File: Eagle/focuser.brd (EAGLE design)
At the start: 52 x 110.2 mm, 50 parts, among them IC1 78xx, J1 J5MM, J10 J5MM, J2 J7MM, J3 J7MM, J4 J5MM, J5 J7MM, J6 J12MM, J7 J7MM, J8 J7MM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

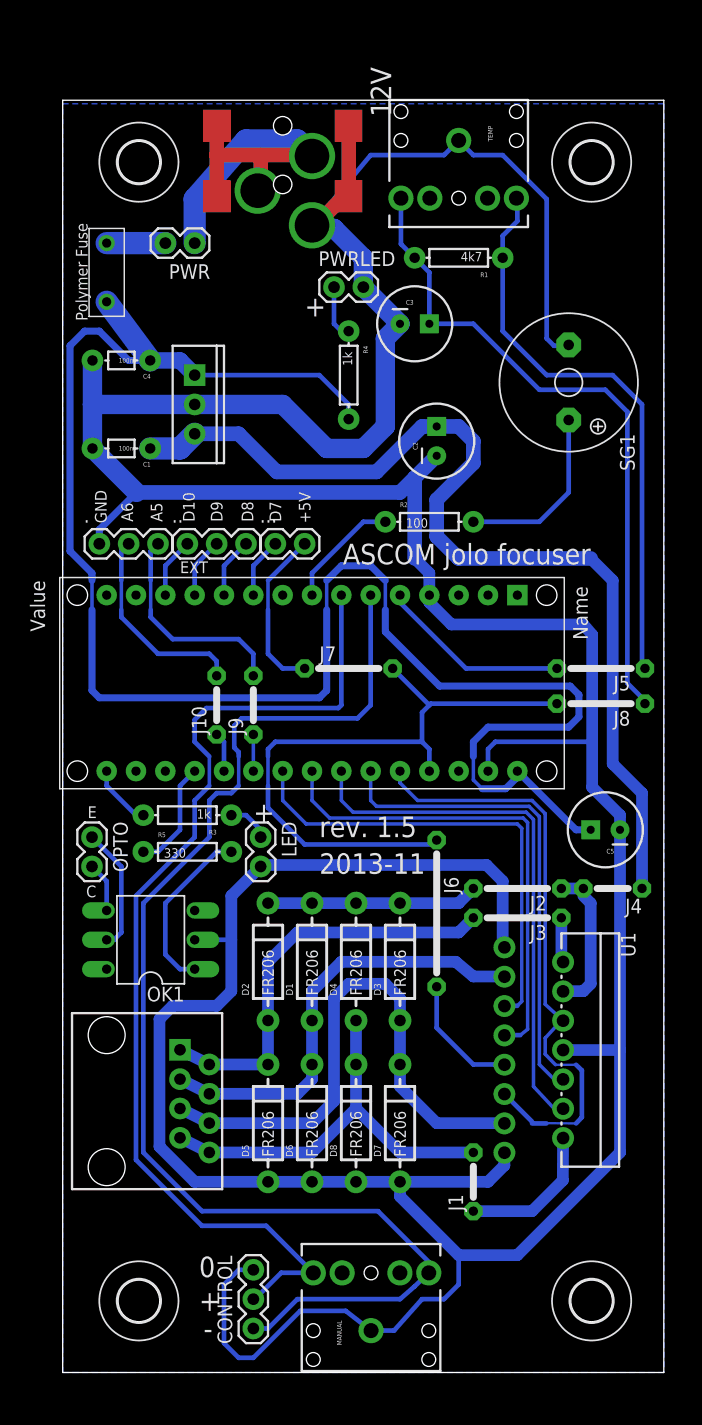
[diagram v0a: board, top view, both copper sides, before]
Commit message: Production PCB refactor
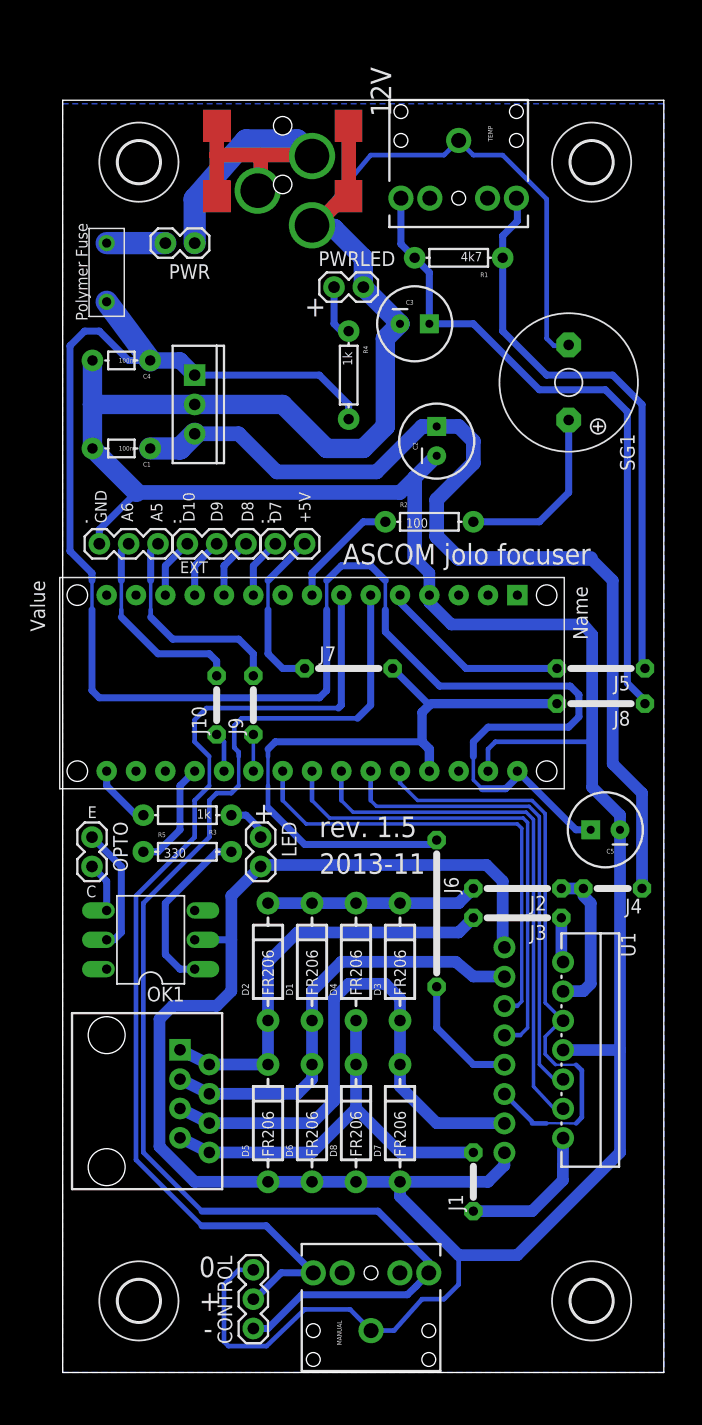
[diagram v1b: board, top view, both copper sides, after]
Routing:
- net GND: track 379.6 -> 378.9 mm

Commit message: Focuser 2.0
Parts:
- removed ...: (no value), SparkFun:1X02
- added ...1: (no value), SparkFun:1X02
- added ..1: (no value), SparkFun:1X03
- added J11: J5MM, jumper:05
- moved J7 19.9 mm to (27.9, 80.6), turned to 90 degrees
- moved C1 19.4 mm to (20.3, 92.1)
- moved . 18.9 mm to (21.6, 76.2), turned to 180 degrees
- moved R4 10.6 mm to (21.6, 96.5), turned to 180 degrees
- moved R1 10.3 mm to (44.5, 94.6)
- moved C4 8.28 mm to (12.1, 92.1), turned to 0 degrees
- moved C3 7.10 mm to (37.5, 89.5)
- moved PWRLED 6.84 mm to (29.8, 96.5)
- moved IC1 6.02 mm to (17.1, 85.7), turned to 0 degrees
- moved .. 5.46 mm to (14.0, 76.2), turned to 180 degrees
- moved SG1 5.43 mm to (45.7, 80.6)
- moved R2 4.45 mm to (36.2, 73.7)
- moved C2 2.54 mm to (34.9, 80.6), turned to 0 degrees
- moved 12V 2.54 mm to (19.1, 110.5)
- moved TEMP 1.90 mm to (34.3, 108.6)
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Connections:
- removed net N$30: C3.1, J8.1, R1.P$2, TEMP.5
- new net N$41: ..1.1, NANO.D10
- new net N$42: ...3, NANO.D11
- new net N$43: ...2, NANO.D12
- new net N$44: C5.1, J11.2, NANO.VIN
- new net N$45: J6.1, J8.2, NANO.+5V
- net +5: now also C3.1, J8.1, R1.P$2, TEMP.5; no longer J6.1, J8.2, NANO.+5V
- net N$18: now also NANO.D6; no longer NANO.D4
- net N$24: now also NANO.D7; no longer NANO.D3
- net N$31: now also ...1; no longer ..2
- net N$32: now also ...1.2, NANO.D4; no longer ...3, NANO.D8
- net N$33: now also ...1.1, NANO.D5; no longer ...2, NANO.D9
- net N$34: now also ..1.3, NANO.D8; no longer ...1, NANO.D10
- net N$35: now also ..1.2, NANO.D9; no longer NANO.D5, R2.P$1
- net N$6: now also ..2; no longer ....2
- net N$8: now also NANO.D3, R2.P$1; no longer ....1, NANO.D7
- net N$9: now also J11.1; no longer C5.1, NANO.VIN
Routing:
- net N$9: track 154.2 -> 91.6 mm
- net N$30: track 58.1 -> 0.00 mm
- net N$45: track 0.00 -> 52.2 mm
- net N$44: track 0.00 -> 48.5 mm
- net +5: track 56.7 -> 85.9 mm
- net N$43: track 0.00 -> 17.3 mm
- net N$42: track 0.00 -> 12.0 mm
- net N$31: track 17.7 -> 28.2 mm
- net GND: track 378.9 -> 369.9 mm
- net N$1: track 15.6 -> 7.26 mm
- net N$24: track 110.2 -> 116.0 mm
- net N$8: track 5.23 -> 10.9 mm
- net VCC2: track 86.1 -> 80.7 mm
- net N$41: track 0.00 -> 5.08 mm
- net N$35: track 10.1 -> 5.08 mm
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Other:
- board size 52 x 110.2 mm -> 54.6 x 113.7 mm
- board text added: "2014-04"
- board text added: "rev. 1.6"
- board text removed: "+5V"
- board text removed: "2013-11"
- board text removed: "A5"
- board text removed: "A6"
- board text removed: "ASCOM jolo focuser"
- board text removed: "D10"
- board text removed: "D7"
- board text removed: "D8"
- board text removed: "D9"
- board text removed: "EXT"
- board text removed: "GND"
- board text removed: "rev. 1.5"

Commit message: Focuser 2.0 - PCB
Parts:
- removed ...1: (no value), SparkFun:1X02
- added ..2: (no value), SparkFun:1X03
- moved IC1 2.54 mm to (14.6, 85.7)
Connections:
- removed net N$40: ..3, J9.2
- removed net VCC: 12V.GND@1, PWR.1
- new net N$30: 12V.POWER, PWR.1
- new net N$46: ..2.1, ..3, J9.2
- net GND: now also 12V.GND@1; no longer 12V.POWER
- net N$32: now also ..2.3; no longer ...1.2
- net N$33: now also ..2.2; no longer ...1.1
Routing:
- net VCC: track 18.6 -> 0.00 mm
- net N$40: track 16.9 -> 0.00 mm
- net N$46: track 0.00 -> 16.9 mm
- net N$30: track 0.00 -> 11.2 mm
- net GND: track 369.9 -> 376.6 mm
- net VCC2: track 80.7 -> 84.7 mm
- net N$9: track 91.6 -> 89.1 mm
- net N$31: track 28.2 -> 27.4 mm
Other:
- board text added: "+5"
- board text added: "A5"
- board text added: "A6"
- board text added: "ASCOM JoloFocuser"
- board text added: "D10"
- board text added: "D11"
- board text added: "D12"
- board text added: "D4"
- board text added: "D5"
- board text added: "D8"
- board text added: "D9"
- board text added: "GND"
- board text added: "rev. 2.0"
- board text removed: "rev. 1.6"

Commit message: Arduino / Eagle updates
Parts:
- removed .: (no value), SparkFun:1X03
- C3, C5: device SparkFun:CPOL-RADIAL-100UF-25V -> resistor:E2-4
- J10, J11: value J5MM -> J7MM; device jumper:05 -> jumper:07
- SG1: device buzzer:F/QMBIII -> buzzer2:F/QMBIII
- moved J9 14.7 mm to (31.1, 56.3), turned to 0 degrees
- moved .. 7.65 mm to (21.6, 75.6)
- moved J11 6.74 mm to (16.1, 59.4)
- moved J10 5.69 mm to (16.1, 62.7), turned to 0 degrees
- moved TEMP 1.55 mm to (34.5, 110.1)
- moved 12V 1.27 mm to (19.1, 111.8)
- moved MANUAL 1.27 mm to (26.7, 1.09)
- moved C3 0.25 mm to (37.7, 89.5), turned to 180 degrees
- moved C5 0.25 mm to (47.2, 47.0), turned to 0 degrees
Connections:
- removed net N$12 (its old number): J9.1, NANO.A5
- removed net N$18 (its old number): CONTROL.2, MANUAL.2, NANO.D6
- removed net N$31 (its old number): ...1, J10.2
- removed net N$46: ..2.1, ..3, J9.2
- new net N$33: NANO.D4, R2.P$1
- new net N$41: J10.2, NANO.A6
- net +5: now also C3.+; no longer C3.1
- net GND: now also ...1, 12V.GND, C3.-, C5.-; no longer ..1, C3.2, C5.2
- net N$13: now also NANO.A2; no longer NANO.A1
- net N$15: now also NANO.A3; no longer NANO.A2
- net N$25: now also ...3, NANO.D12; no longer J10.1, NANO.A6
- net N$3: now also J9.2; no longer NANO.A0
- net N$32: now also NANO.D3; no longer NANO.D4
- net N$35: now also ..2.1, NANO.D6; no longer ..1.3, NANO.D8
- net N$4: now also NANO.A5; no longer NANO.A4
- net N$42: now also J9.1; no longer ...3
- net N$43: now also ..1.3, J10.1; no longer ...2, NANO.D12
- net N$44: now also C5.+; no longer C5.1
- net N$5: now also NANO.A4; no longer NANO.A3
- net N$6: now also ...2; no longer ..2
- net N$8: now also CONTROL.2, MANUAL.2, NANO.D8; no longer NANO.D3, R2.P$1
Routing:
- net N$18 (its old number): track 89.4 -> 0.00 mm
- net N$8: track 10.9 -> 94.2 mm
- net N$42: track 12.0 -> 44.3 mm
- net N$31 (its old number): track 27.4 -> 0.00 mm
- net GND: track 376.6 -> 397.1 mm
- net N$25: track 3.44 -> 22.0 mm
- net N$46: track 16.9 -> 0.00 mm
- net N$40: track 115.8 -> 99.3 mm
- net N$41: track 0.00 -> 14.3 mm
- net N$9: track 89.1 -> 77.2 mm
- net N$43: track 17.3 -> 28.8 mm
- net N$33: track 0.00 -> 11.3 mm
- net N$32: track 6.13 -> 14.4 mm
- net N$44: track 48.5 -> 54.3 mm
- net N$45: track 52.2 -> 56.2 mm
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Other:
- board size 54.6 x 113.7 mm -> 54.6 x 116.2 mm
- board text added: "A2"
- board text added: "D13"
- board text added: "D3"
- board text added: "D6"
- board text removed: "A5"
- board text removed: "A6"
- board text removed: "D11"
- board text removed: "D12"
- board text removed: "D4"
- board text removed: "D8"
